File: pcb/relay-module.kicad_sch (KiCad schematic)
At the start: 41 parts, among them J1 AVR-UPDI-6, J2 QWICC, J3 Power In, J4 Power Out, K1 PR24-5V-900-1A, P1 MountingHole_Pad, P2 MountingHole_Pad, P3 MountingHole_Pad, P4 MountingHole_Pad, Q1 MMBT3904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

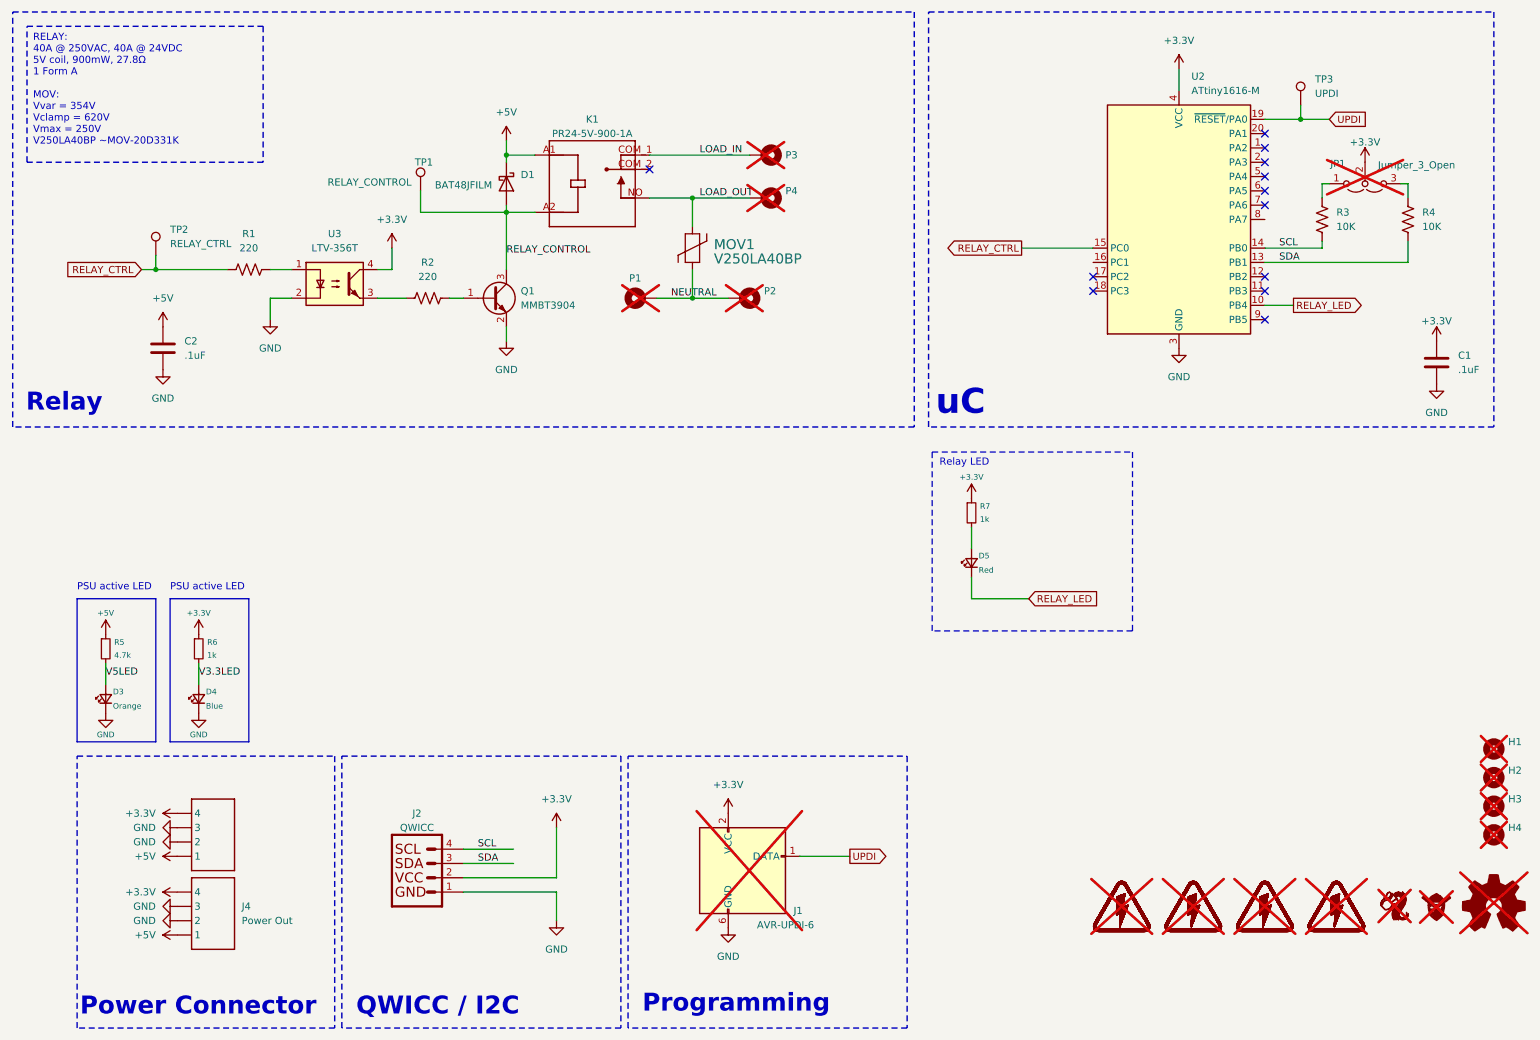
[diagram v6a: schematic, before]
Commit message: Refined relay based testing
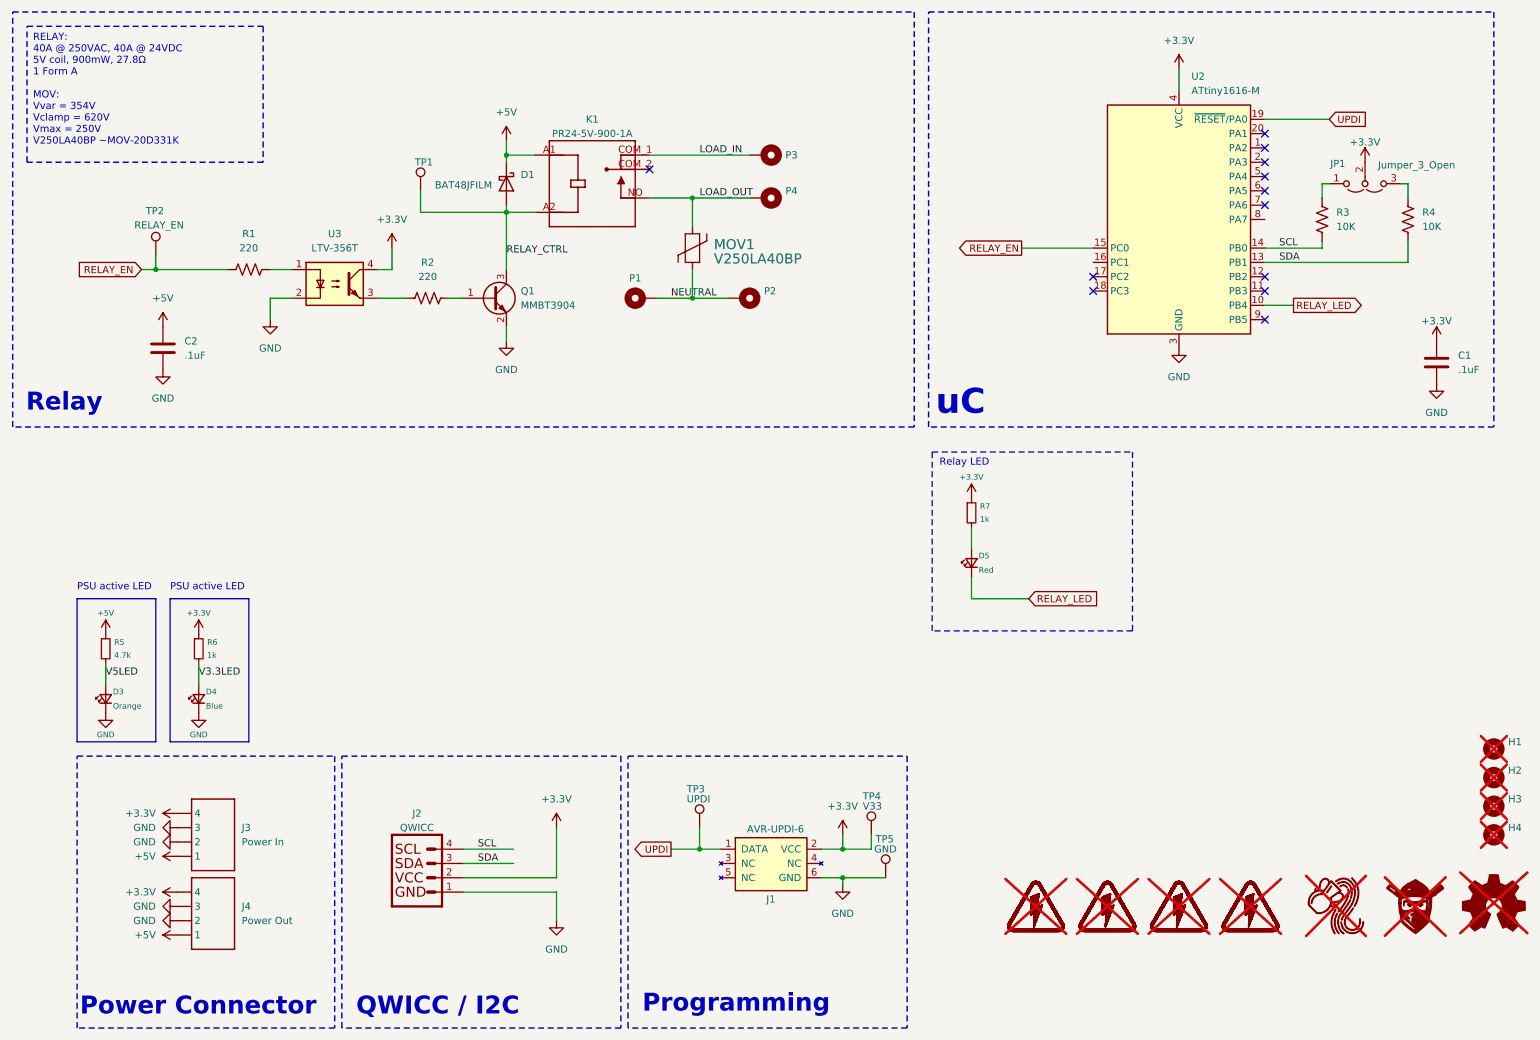
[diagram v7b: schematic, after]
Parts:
- added TP4: V33, TestPoint:TestPoint_Pad_D1.0mm, symbol Connector:TestPoint
- added TP5: GND, TestPoint:TestPoint_Pad_D1.0mm, symbol Connector:TestPoint
- J1: footprint Connector_PinHeader_2.54mm:PinHeader_2x03_P2.54mm_Vertical -> CRGM Connector:PinHeader_2x03_P2.54mm_Vertical_SMD; symbol Connector:AVR-UPDI-6 -> CRGM Connector:AVR-UPDI-6; now fitted
- JP1, P1, P2, P3, P4: now fitted
- LOGO1: footprint CRGM Logos:Aquarius Logo 5mm -> CRGM Logos:Aquarius Logo 10mm
- LOGO3: footprint CRGM Logos:FNWW Face 5mm -> CRGM Logos:FNWW Face 10mm
- TP1: value RELAY_CONTROL -> RELAY_CTRL
- TP2: value RELAY_CTRL -> RELAY_EN
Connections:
- net RELAY_CONTROL is gone; now on net RELAY_CTRL: D1.2 (A), K1.A2 (COIL2), Q1.3 (C), TP1.1
- net +3.3V: now also TP4.1
- net GND: now also TP5.1
- net RELAY_CTRL: no longer R1.1, TP2.1, U2.15 (PC0)
- new net RELAY_EN: R1.1, TP2.1, U2.15 (PC0)
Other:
- moved on the sheet: TP3

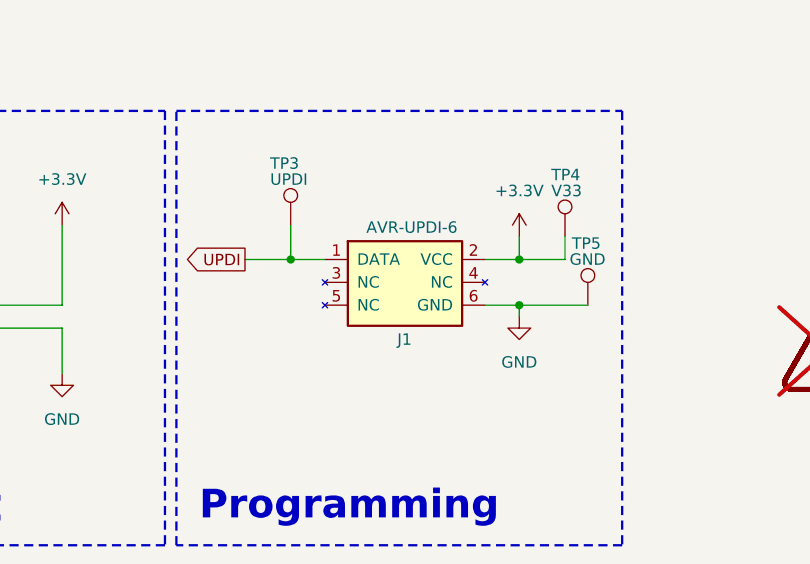
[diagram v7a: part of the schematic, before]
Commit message: Fixed missing LCSC part numbers; updated CI script
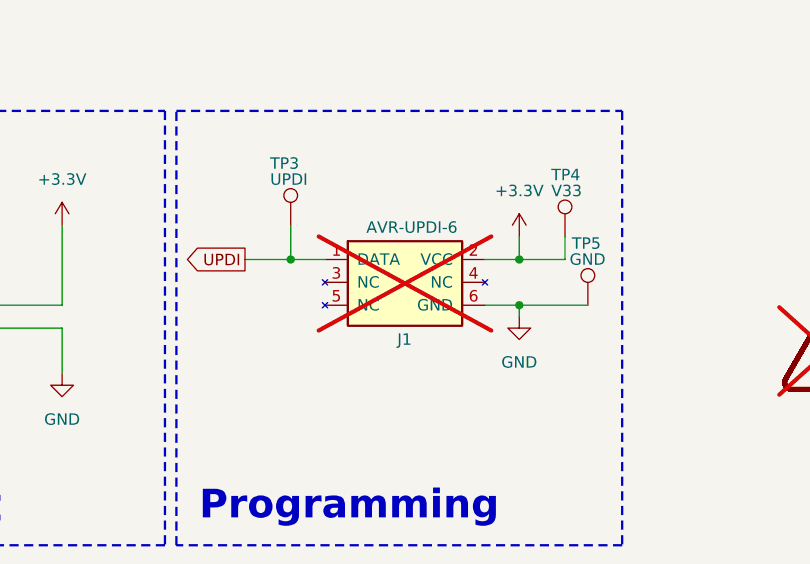
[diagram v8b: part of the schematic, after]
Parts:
- C1, C2: LCSC (none) -> C15849; MPN (none) -> CL10A105KB8NNNC
- D1: LCSC (none) -> C2798199; MN (none) -> STMicroelectronics; MPN (none) -> BAT48JFILM
- J1: now not fitted
- J2, J3, J4: footprint CRGM Connector:SM04B-SRSS-TB -> CRGM Connector:JST_SH_SM04B-SRSS-TB_1x04-1MP_P1.00mm_Horizontal; Digikey (none) -> 455-SM04B-SRSS-TBTR-ND; Mouser (none) -> 306-SM04BSRSSTBTLFSN
- Q1: MN (none) -> GOODWORK
- R1, R2: LCSC (none) -> C22962; MN (none) -> Uni-Royal; MPN (none) -> 0603WAF2200T5E
- R3, R4: LCSC (none) -> C25804; MN (none) -> Uni-Royal; MPN (none) -> 0603WAF1002T5E
- U2: LCSC (none) -> C507118; MN (none) -> Microchip Tech; MPN (none) -> ATTINY1616-MNR
- U3: LCSC (none) -> C125117; MN (none) -> Lite-On; MPN (none) -> LTV-356T
